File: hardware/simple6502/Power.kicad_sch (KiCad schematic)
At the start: 6 parts, among them J5 Barrel_Jack_Switch

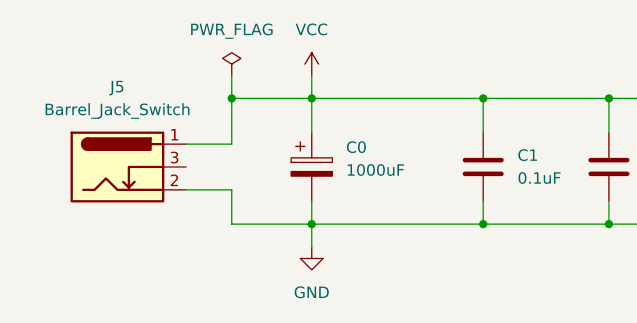
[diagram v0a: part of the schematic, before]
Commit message: Fixed Bus label names
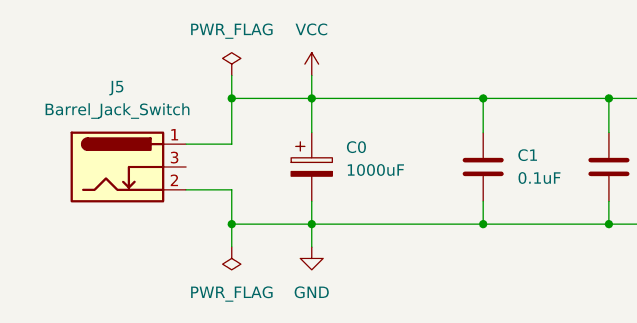
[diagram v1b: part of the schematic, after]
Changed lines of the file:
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@@
   (junction (at 93.98 27.94) (diameter 0) (color 0 0 0 0)
+  )
+  (junction (at 38.1 41.91) (diameter 0) (color 0 0 0 0)
   )
   (junction (at 93.98 41.91) (diameter 0) (color 0 0 0 0)
@@
     (stroke (width 0) (type default))
   )
+  (wire (pts (xy 38.1 44.45) (xy 38.1 41.91))
+    (stroke (width 0) (type default))
+  )
   (wire (pts (xy 80.01 39.37) (xy 80.01 41.91))
     (stroke (width 0) (type default))
@@
     (stroke (width 0) (type default))
   )
+  (symbol (lib_id "power:PWR_FLAG") (at 38.1 44.45 180) (unit 1)
+    (in_bom yes) (on_board yes) (dnp no) (fields_autoplaced)
+    (property "Reference" "#FLG02" (at 38.1 46.355 0)
+      (effects (font (size 1.27 1.27)) hide)
+    )
+    (property "Value" "PWR_FLAG" (at 38.1 49.53 0)
+      (effects (font (size 1.27 1.27)))
+    )
+    (property "Footprint" "" (at 38.1 44.45 0)
+      (effects (font (size 1.27 1.27)) hide)
+    )
+    (property "Datasheet" "~" (at 38.1 44.45 0)
+      (effects (font (size 1.27 1.27)) hide)
+    )
+    (pin "1")
+    (instances
+      (project "simple6502"
+        (path "/c0007eb4-077e-4f77-aad9-8dd15548af06/710f29f6-117a-4dcb-a5e3-826b377de52e"
+          (reference "#FLG02") (unit 1)
+        )
+      )
+    )
+  )
   (symbol (lib_id "Device:C_Polarized") (at 46.99 35.56 0) (unit 1)

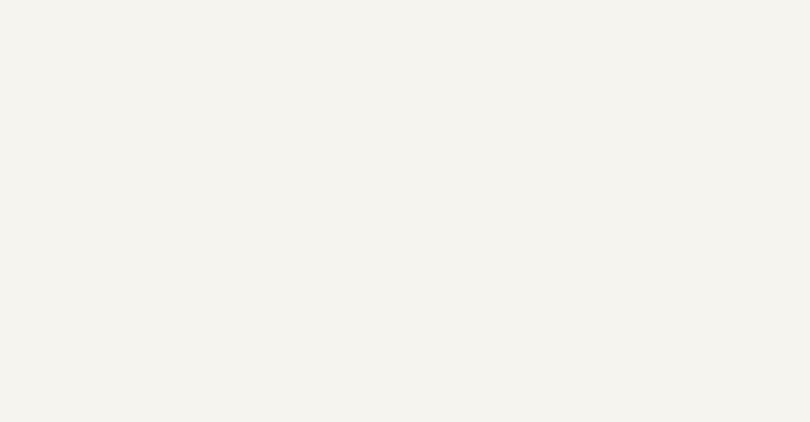
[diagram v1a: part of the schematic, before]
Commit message: Memory decoder v1
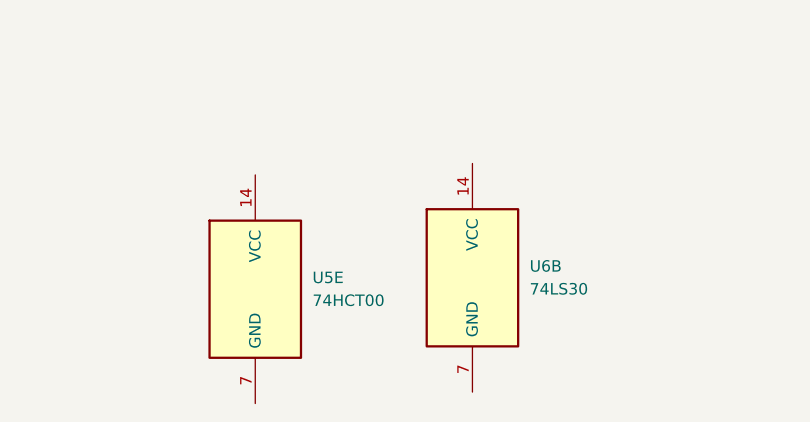
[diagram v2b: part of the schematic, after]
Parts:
- added U5: 74HCT00, symbol 74xx:74HCT00
- added U6: 74LS30, symbol 74xx:74LS30
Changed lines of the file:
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@@
+    )
+  )
+  (symbol (lib_id "74xx:74HCT00") (at 49.53 83.82 0) (unit 5)
+    (in_bom yes) (on_board yes) (dnp no) (fields_autoplaced)
+    (property "Reference" "U5" (at 55.88 82.55 0)
+      (effects (font (size 1.27 1.27)) (justify left))
+    )
+    (property "Value" "74HCT00" (at 55.88 85.09 0)
+      (effects (font (size 1.27 1.27)) (justify left))
+    )
+    (property "Footprint" "" (at 49.53 83.82 0)
+      (effects (font (size 1.27 1.27)) hide)
+    )
+    (property "Datasheet" "http://www.ti.com/lit/gpn/sn74hct00" (at 49.53 83.82 0)
+      (effects (font (size 1.27 1.27)) hide)
+    )
+    (pin "1")
+    (pin "2")
+    (pin "3")
+    (pin "4")
+    (pin "5")
+    (pin "6")
+    (pin "10")
+    (pin "8")
+    (pin "9")
+    (pin "11")
+    (pin "12")
+    (pin "13")
+    (pin "14")
+    (pin "7")
+    (instances
+      (project "simple6502"
+        (path "/c0007eb4-077e-4f77-aad9-8dd15548af06"
+          (reference "U5") (unit 5)
+        )
+        (path "/c0007eb4-077e-4f77-aad9-8dd15548af06/710f29f6-117a-4dcb-a5e3-826b377de52e"
+          (reference "U5") (unit 5)
+        )
+      )
     )
   )
@@
         )
       )
+    )
+  )
+  (symbol (lib_id "74xx:74LS30") (at 73.66 82.55 0) (unit 2)
+    (in_bom yes) (on_board yes) (dnp no) (fields_autoplaced)
+    (property "Reference" "U6" (at 80.01 81.28 0)
+      (effects (font (size 1.27 1.27)) (justify left))
+    )
+    (property "Value" "74LS30" (at 80.01 83.82 0)
+      (effects (font (size 1.27 1.27)) (justify left))
+    )
+    (property "Footprint" "" (at 73.66 82.55 0)
+      (effects (font (size 1.27 1.27)) hide)
+    )
+    (property "Datasheet" "http://www.ti.com/lit/gpn/sn74LS30" (at 73.66 82.55 0)
+      (effects (font (size 1.27 1.27)) hide)
+    )
+    (pin "1")
+    (pin "11")
+    (pin "12")
+    (pin "2")
+    (pin "3")
+    (pin "4")
+    (pin "5")
+    (pin "6")
+    (pin "8")
+    (pin "14")
+    (pin "7")
+    (instances
+      (project "simple6502"
+        (path "/c0007eb4-077e-4f77-aad9-8dd15548af06"
+          (reference "U6") (unit 2)
+        )
+        (path "/c0007eb4-077e-4f77-aad9-8dd15548af06/710f29f6-117a-4dcb-a5e3-826b377de52e"
+          (reference "U6") (unit 2)
+        )
+      )

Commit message: Main board schematic complete v0.0.1
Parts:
- removed C0: 1000uF, symbol Device:C_Polarized
- removed C1: 0.1uF, symbol Device:C
- added C1: 1000uF, symbol Device:C_Polarized
- added C5, C6, C7: 0.1uF, symbol Device:C
- added D1: LED, symbol Device:LED
- added H1, H2, H3, H4: MountingHole_Pad, symbol Mechanical:MountingHole_Pad
- added J6: AUX 5VDC, symbol Connector:Conn_01x03_Pin
- added R6: 220, symbol Device:R
- added SW2: POWER, symbol Switch:SW_Push_DPDT
- J5: value Barrel_Jack_Switch -> POWER 5V
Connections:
- net GND: now also U5.7 (GND), U6.7 (GND), C1.2, C5.2, C6.2, C7.2, H1.1, H2.1, H3.1, H4.1, R6.2
- net VCC: now also U5.14 (VCC), U6.14 (VCC), C1.1, C5.1, C6.1, C7.1, D1.2 (A), SW2.1 (A), SW2.4 (A); no longer J5.1
- net at J5.3: now also J6.1 (Pin_1), J6.3 (Pin_3)
- new net: D1.1 (K), R6.1
- new net: J5.1, J6.2 (Pin_2), SW2.2 (B), SW2.5 (B)
- no-connect marks 0 -> 2
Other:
- note added: "Mounting Holes"
- note added: "Power Input"
- moved on the sheet: J5, U5E, U6B

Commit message: Footprint round 1
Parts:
- C1: footprint (none) -> Capacitor_THT:CP_Radial_D6.3mm_P2.50mm
- C2, C3, C4, C5, C6, C7: footprint (none) -> Capacitor_THT:C_Rect_L4.0mm_W2.5mm_P2.50mm
- D1: footprint (none) -> LED_THT:LED_D3.0mm
- H1, H2, H3, H4: footprint (none) -> MountingHole:MountingHole_2.7mm_M2.5_Pad_Via
- J5: footprint (none) -> Connector_BarrelJack:BarrelJack_Horizontal
- J6: footprint (none) -> Connector_PinHeader_2.54mm:PinHeader_1x03_P2.54mm_Vertical
- R6: footprint (none) -> Resistor_THT:R_Axial_DIN0204_L3.6mm_D1.6mm_P7.62mm_Horizontal
- SW2: footprint (none) -> Button_Switch_THT:SW_Push_2P2T_Toggle_CK_PVA2OAH5xxxxxxV2
- U5, U6: footprint (none) -> Package_DIP:DIP-14_W7.62mm_Socket
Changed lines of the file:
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@@
   (symbol (lib_id "power:PWR_FLAG") (at 46.99 53.34 180) (unit 1)
     (in_bom yes) (on_board yes) (dnp no) (fields_autoplaced)
-    (property "Reference" "#FLGGND" (at 46.99 55.245 0)
+    (property "Reference" "#FLGGND0101" (at 46.99 55.245 0)
       (effects (font (size 1.27 1.27)) hide)
     )
@@
       (project "simple6502"
         (path "/c0007eb4-077e-4f77-aad9-8dd15548af06/710f29f6-117a-4dcb-a5e3-826b377de52e"
-          (reference "#FLGGND") (unit 1)
+          (reference "#FLGGND0101") (unit 1)
         )
       )
@@
       (effects (font (size 1.27 1.27)) (justify left))
     )
-    (property "Footprint" "" (at 150.8252 85.09 0)
+    (property "Footprint" "Capacitor_THT:C_Rect_L4.0mm_W2.5mm_P2.50mm" (at 150.8252 85.09 0)
       (effects (font (size 1.27 1.27)) hide)
     )
@@
       (effects (font (size 1.27 1.27)) (justify left))
     )
-    (property "Footprint" "" (at 22.352 93.98 90)
+    (property "Footprint" "Resistor_THT:R_Axial_DIN0204_L3.6mm_D1.6mm_P7.62mm_Horizontal" (at 22.352 93.98 90)
       (effects (font (size 1.27 1.27)) hide)
     )
@@
       (effects (font (size 1.27 1.27)) (justify left))
     )
-    (property "Footprint" "" (at 194.0052 85.09 0)
+    (property "Footprint" "Capacitor_THT:C_Rect_L4.0mm_W2.5mm_P2.50mm" (at 194.0052 85.09 0)
       (effects (font (size 1.27 1.27)) hide)
     )
@@
       (effects (font (size 1.27 1.27)))
     )
-    (property "Footprint" "" (at 31.75 49.276 0)
+    (property "Footprint" "Connector_BarrelJack:BarrelJack_Horizontal" (at 31.75 49.276 0)
       (effects (font (size 1.27 1.27)) hide)
     )
@@
       (effects (font (size 1.27 1.27)) (justify left))
     )
-    (property "Footprint" "" (at 133.35 39.37 0)
+    (property "Footprint" "Package_DIP:DIP-14_W7.62mm_Socket" (at 133.35 39.37 0)
       (effects (font (size 1.27 1.27)) hide)
     )
@@
       (effects (font (size 1.27 1.27)) (justify left))
     )
-    (property "Footprint" "" (at 103.8352 85.09 0)
+    (property "Footprint" "Capacitor_THT:CP_Radial_D6.3mm_P2.50mm" (at 103.8352 85.09 0)
       (effects (font (size 1.27 1.27)) hide)
     )
@@
       (effects (font (size 1.27 1.27)) (justify left))
     )
-    (property "Footprint" "" (at 122.8852 85.09 0)
+    (property "Footprint" "Capacitor_THT:C_Rect_L4.0mm_W2.5mm_P2.50mm" (at 122.8852 85.09 0)
       (effects (font (size 1.27 1.27)) hide)
     )
@@
       (effects (font (size 1.27 1.27)) (justify left) hide)
     )
-    (property "Footprint" "" (at 53.34 91.44 0)
+    (property "Footprint" "MountingHole:MountingHole_2.7mm_M2.5_Pad_Via" (at 53.34 91.44 0)
       (effects (font (size 1.27 1.27)) hide)
     )
@@
       (effects (font (size 1.27 1.27)) (justify left))
     )
-    (property "Footprint" "" (at 178.7652 85.09 0)
+    (property "Footprint" "Capacitor_THT:C_Rect_L4.0mm_W2.5mm_P2.50mm" (at 178.7652 85.09 0)
       (effects (font (size 1.27 1.27)) hide)
     )
@@
       (effects (font (size 1.27 1.27)) (justify left))
     )
-    (property "Footprint" "" (at 156.21 39.37 0)
+    (property "Footprint" "Package_DIP:DIP-14_W7.62mm_Socket" (at 156.21 39.37 0)
       (effects (font (size 1.27 1.27)) hide)
     )
@@
       (effects (font (size 1.27 1.27)) (justify left) hide)
     )
-    (property "Footprint" "" (at 53.34 82.55 0)
+    (property "Footprint" "MountingHole:MountingHole_2.7mm_M2.5_Pad_Via" (at 53.34 82.55 0)
       (effects (font (size 1.27 1.27)) hide)
     )
@@
       (effects (font (size 1.27 1.27)) (justify left) hide)
     )
-    (property "Footprint" "" (at 43.18 82.55 0)
+    (property "Footprint" "MountingHole:MountingHole_2.7mm_M2.5_Pad_Via" (at 43.18 82.55 0)
       (effects (font (size 1.27 1.27)) hide)
     )
@@
       (effects (font (size 1.27 1.27)) (justify left) hide)
     )
-    (property "Footprint" "" (at 43.18 91.44 0)
+    (property "Footprint" "MountingHole:MountingHole_2.7mm_M2.5_Pad_Via" (at 43.18 91.44 0)
       (effects (font (size 1.27 1.27)) hide)
     )
@@
       (effects (font (size 1.27 1.27)) (justify left))
     )
-    (property "Footprint" "" (at 136.8552 85.09 0)
+    (property "Footprint" "Capacitor_THT:C_Rect_L4.0mm_W2.5mm_P2.50mm" (at 136.8552 85.09 0)
       (effects (font (size 1.27 1.27)) hide)
     )
@@
       (effects (font (size 1.27 1.27)))
     )
-    (property "Footprint" "" (at 77.47 45.72 0)
+    (property "Footprint" "Button_Switch_THT:SW_Push_2P2T_Toggle_CK_PVA2OAH5xxxxxxV2" (at 77.47 45.72 0)
       (effects (font (size 1.27 1.27)) hide)
     )
@@
       (effects (font (size 1.27 1.27)) (justify right))
     )
-    (property "Footprint" "" (at 24.13 83.82 0)
+    (property "Footprint" "LED_THT:LED_D3.0mm" (at 24.13 83.82 0)
       (effects (font (size 1.27 1.27)) hide)
     )
@@
       (effects (font (size 1.27 1.27)) (justify left))
     )
-    (property "Footprint" "" (at 164.7952 85.09 0)
+    (property "Footprint" "Capacitor_THT:C_Rect_L4.0mm_W2.5mm_P2.50mm" (at 164.7952 85.09 0)
       (effects (font (size 1.27 1.27)) hide)
     )
@@
       (effects (font (size 1.27 1.27)))
     )
-    (property "Footprint" "" (at 46.99 31.75 0)
-      (effects (font (size 1.27 1.27)) hide)
-    )
+    (property "Footprint" "Connector_PinHeader_2.54mm:PinHeader_1x03_P2.54mm_Vertical" (at 46.99 31.75 0)
+      (effects (font (size 1.27 1.27)) hide)
+    )

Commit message: v0.5 Schematic complete and footprint assigned.
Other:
- company: (none) -> Mariano Luna
- title: (none) -> simple6502
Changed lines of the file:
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@@
 (kicad_sch (version 20230121) (generator eeschema)
   (paper "A4")
+  (title_block
+    (title "simple6502")
+    (date "2023-09-23")
+    (rev "0.5")
+    (company "Mariano Luna")
+  )
   (junction (at 44.45 41.91) (diameter 0) (color 0 0 0 0)
   )

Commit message: PCB defaults set and components dropped
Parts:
- added SLOT1, SLOT2: 6502 BUS, Connector_Card:EDAC 395-050-520-201, symbol Connector_Generic:Conn_02x25_Counter_Clockwise
- H1, H2, H3, H4: value MountingHole_Pad -> M
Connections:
- net GND: now also SLOT1.25 (Pin_25), SLOT1.39 (Pin_39), SLOT1.50 (Pin_50), SLOT2.25 (Pin_25), SLOT2.39 (Pin_39), SLOT2.50 (Pin_50)
- net VCC: now also SLOT1.1 (Pin_1), SLOT1.26 (Pin_26), SLOT2.1 (Pin_1), SLOT2.26 (Pin_26)
- net 5VDC IN: now reaches J5.1, J6.2 (Pin_2), SW2.2 (B), SW2.5 (B)
- net AUX GND: now reaches J5.3, J6.1 (Pin_1), J6.3 (Pin_3)
- new net A0: SLOT1.2 (Pin_2), SLOT2.2 (Pin_2)
- new net A1: SLOT1.3 (Pin_3), SLOT2.3 (Pin_3)
- new net A10: SLOT1.44 (Pin_44), SLOT2.44 (Pin_44)
- new net A11: SLOT1.45 (Pin_45), SLOT2.45 (Pin_45)
- new net A12: SLOT1.46 (Pin_46), SLOT2.46 (Pin_46)
- new net A13: SLOT1.47 (Pin_47), SLOT2.47 (Pin_47)
- new net A14: SLOT1.48 (Pin_48), SLOT2.48 (Pin_48)
- new net A15: SLOT1.49 (Pin_49), SLOT2.49 (Pin_49)
- new net A2: SLOT1.4 (Pin_4), SLOT2.4 (Pin_4)
- new net A3: SLOT1.5 (Pin_5), SLOT2.5 (Pin_5)
- new net A4: SLOT1.6 (Pin_6), SLOT2.6 (Pin_6)
- new net A5: SLOT1.7 (Pin_7), SLOT2.7 (Pin_7)
- new net A6: SLOT1.8 (Pin_8), SLOT2.8 (Pin_8)
- new net A7: SLOT1.9 (Pin_9), SLOT2.9 (Pin_9)
- new net A8: SLOT1.42 (Pin_42), SLOT2.42 (Pin_42)
- new net A9: SLOT1.43 (Pin_43), SLOT2.43 (Pin_43)
- new net CLK: SLOT1.24 (Pin_24), SLOT2.24 (Pin_24)
- new net D0: SLOT1.10 (Pin_10), SLOT2.10 (Pin_10)
- new net D1: SLOT1.11 (Pin_11), SLOT2.11 (Pin_11)
- new net D2: SLOT1.12 (Pin_12), SLOT2.12 (Pin_12)
- new net D3: SLOT1.13 (Pin_13), SLOT2.13 (Pin_13)
- new net D4: SLOT1.14 (Pin_14), SLOT2.14 (Pin_14)
- new net D5: SLOT1.15 (Pin_15), SLOT2.15 (Pin_15)
- new net D6: SLOT1.16 (Pin_16), SLOT2.16 (Pin_16)
- new net D7: SLOT1.17 (Pin_17), SLOT2.17 (Pin_17)
- new net ~{IO_CS}: SLOT1.36 (Pin_36), SLOT2.36 (Pin_36)
- new net ~{IRQ}: SLOT1.23 (Pin_23), SLOT2.23 (Pin_23)
- new net ~{NMI}: SLOT1.28 (Pin_28), SLOT2.28 (Pin_28)
- new net ~{RAM_CS}: SLOT1.38 (Pin_38), SLOT2.38 (Pin_38)
- new net ~{RD}: SLOT1.41 (Pin_41), SLOT2.41 (Pin_41)
- new net ~{RESET}: SLOT1.27 (Pin_27), SLOT2.27 (Pin_27)
- new net ~{ROM_CS}: SLOT1.37 (Pin_37), SLOT2.37 (Pin_37)
- new net ~{WR}: SLOT1.40 (Pin_40), SLOT2.40 (Pin_40)
- no-connect marks 2 -> 26
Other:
- note added: "BUS Connector: EDAC 395-050-520-201"
- moved on the sheet: C1, C2, C3, C4, C5, C6, C7, D1, H1, H2, H3, H4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

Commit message: Fixed Apple Connector 3D model, routing started
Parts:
- C2, C3, C4, C5, C6, C7: footprint Capacitor_THT:C_Rect_L4.0mm_W2.5mm_P2.50mm -> Capacitor_THT:C_Disc_D3.0mm_W1.6mm_P2.50mm
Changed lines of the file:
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@@
       (effects (font (size 1.27 1.27)) (justify left))
     )
-    (property "Footprint" "Capacitor_THT:C_Rect_L4.0mm_W2.5mm_P2.50mm" (at 230.8352 40.64 0)
+    (property "Footprint" "Capacitor_THT:C_Disc_D3.0mm_W1.6mm_P2.50mm" (at 230.8352 40.64 0)
       (effects (font (size 1.27 1.27)) hide)
     )
@@
       (effects (font (size 1.27 1.27)) (justify left))
     )
-    (property "Footprint" "Capacitor_THT:C_Rect_L4.0mm_W2.5mm_P2.50mm" (at 274.0152 40.64 0)
+    (property "Footprint" "Capacitor_THT:C_Disc_D3.0mm_W1.6mm_P2.50mm" (at 274.0152 40.64 0)
       (effects (font (size 1.27 1.27)) hide)
     )
@@
       (effects (font (size 1.27 1.27)) (justify left))
     )
-    (property "Footprint" "Capacitor_THT:C_Rect_L4.0mm_W2.5mm_P2.50mm" (at 202.8952 40.64 0)
+    (property "Footprint" "Capacitor_THT:C_Disc_D3.0mm_W1.6mm_P2.50mm" (at 202.8952 40.64 0)
       (effects (font (size 1.27 1.27)) hide)
     )
@@
       (effects (font (size 1.27 1.27)) (justify left))
     )
-    (property "Footprint" "Capacitor_THT:C_Rect_L4.0mm_W2.5mm_P2.50mm" (at 258.7752 40.64 0)
+    (property "Footprint" "Capacitor_THT:C_Disc_D3.0mm_W1.6mm_P2.50mm" (at 258.7752 40.64 0)
       (effects (font (size 1.27 1.27)) hide)
     )
@@
       (effects (font (size 1.27 1.27)) (justify left))
     )
-    (property "Footprint" "Capacitor_THT:C_Rect_L4.0mm_W2.5mm_P2.50mm" (at 216.8652 40.64 0)
+    (property "Footprint" "Capacitor_THT:C_Disc_D3.0mm_W1.6mm_P2.50mm" (at 216.8652 40.64 0)
       (effects (font (size 1.27 1.27)) hide)
     )
@@
       (effects (font (size 1.27 1.27)) (justify left))
     )
-    (property "Footprint" "Capacitor_THT:C_Rect_L4.0mm_W2.5mm_P2.50mm" (at 244.8052 40.64 0)
-      (effects (font (size 1.27 1.27)) hide)
-    )
+    (property "Footprint" "Capacitor_THT:C_Disc_D3.0mm_W1.6mm_P2.50mm" (at 244.8052 40.64 0)
+      (effects (font (size 1.27 1.27)) hide)
+    )

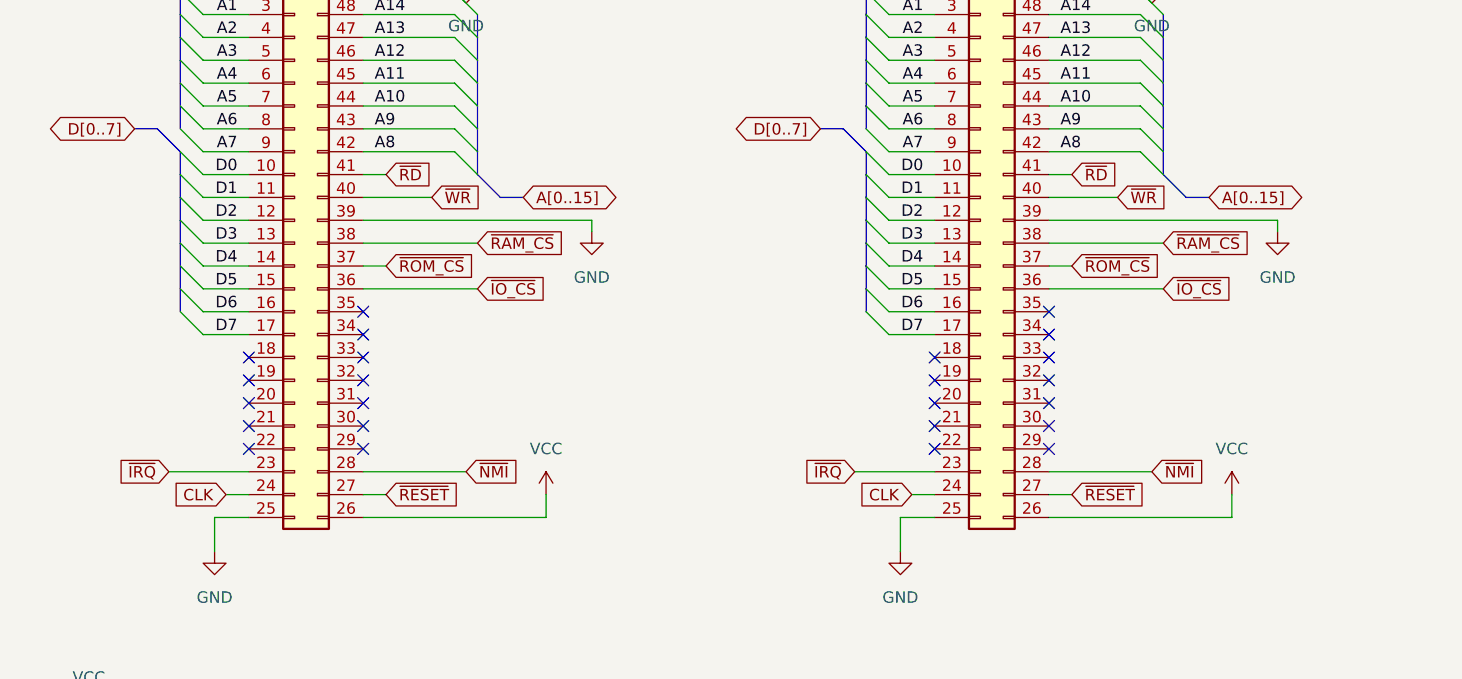
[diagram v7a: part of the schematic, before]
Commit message: rearange the bus for better routing
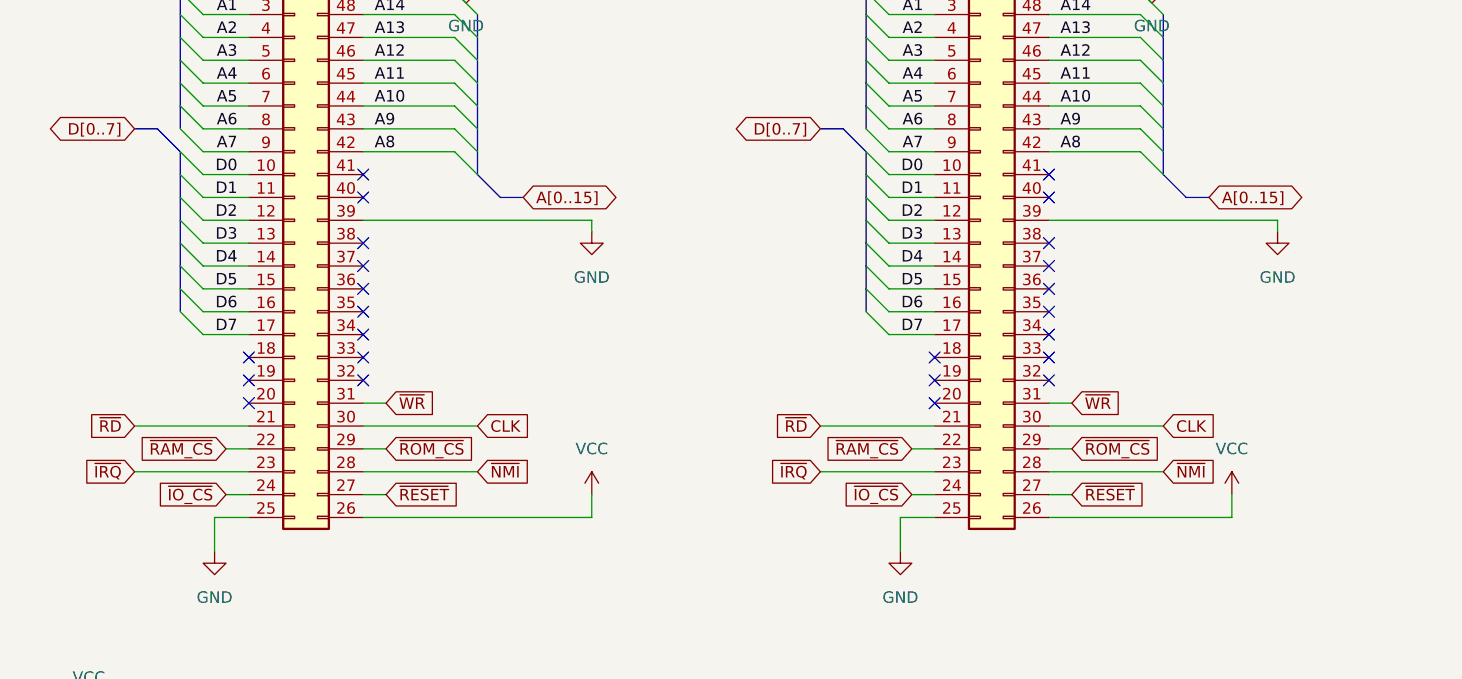
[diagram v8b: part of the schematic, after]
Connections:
- net CLK: now also SLOT1.30 (Pin_30), SLOT2.30 (Pin_30); no longer SLOT1.24 (Pin_24), SLOT2.24 (Pin_24)
- net ~{IO_CS}: now also SLOT1.24 (Pin_24), SLOT2.24 (Pin_24); no longer SLOT1.36 (Pin_36), SLOT2.36 (Pin_36)
- net ~{RAM_CS}: now also SLOT1.22 (Pin_22), SLOT2.22 (Pin_22); no longer SLOT1.38 (Pin_38), SLOT2.38 (Pin_38)
- net ~{RD}: now also SLOT1.21 (Pin_21), SLOT2.21 (Pin_21); no longer SLOT1.41 (Pin_41), SLOT2.41 (Pin_41)
- net ~{ROM_CS}: now also SLOT1.29 (Pin_29), SLOT2.29 (Pin_29); no longer SLOT1.37 (Pin_37), SLOT2.37 (Pin_37)
- net ~{WR}: now also SLOT1.31 (Pin_31), SLOT2.31 (Pin_31); no longer SLOT1.40 (Pin_40), SLOT2.40 (Pin_40)
